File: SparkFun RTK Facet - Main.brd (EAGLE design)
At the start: 60 x 40 mm, 119 parts, among them J17 3-PIN SMD, J18 QWIIC_RIGHT_ANGLE, J2 U.FL, J3 Qwiic, J4 Qwiic Right Angle, Q1 600mA/40V, Q2 MBT3904DW1T1, U1 74HC4052D, U10 MCP73833, U2 3.3V, U3 U-BLOX_ZED-F9P, U4 3.3V, U5 ESP-WROOM-32NARROW, U6 CH340C, U7 MAX17048

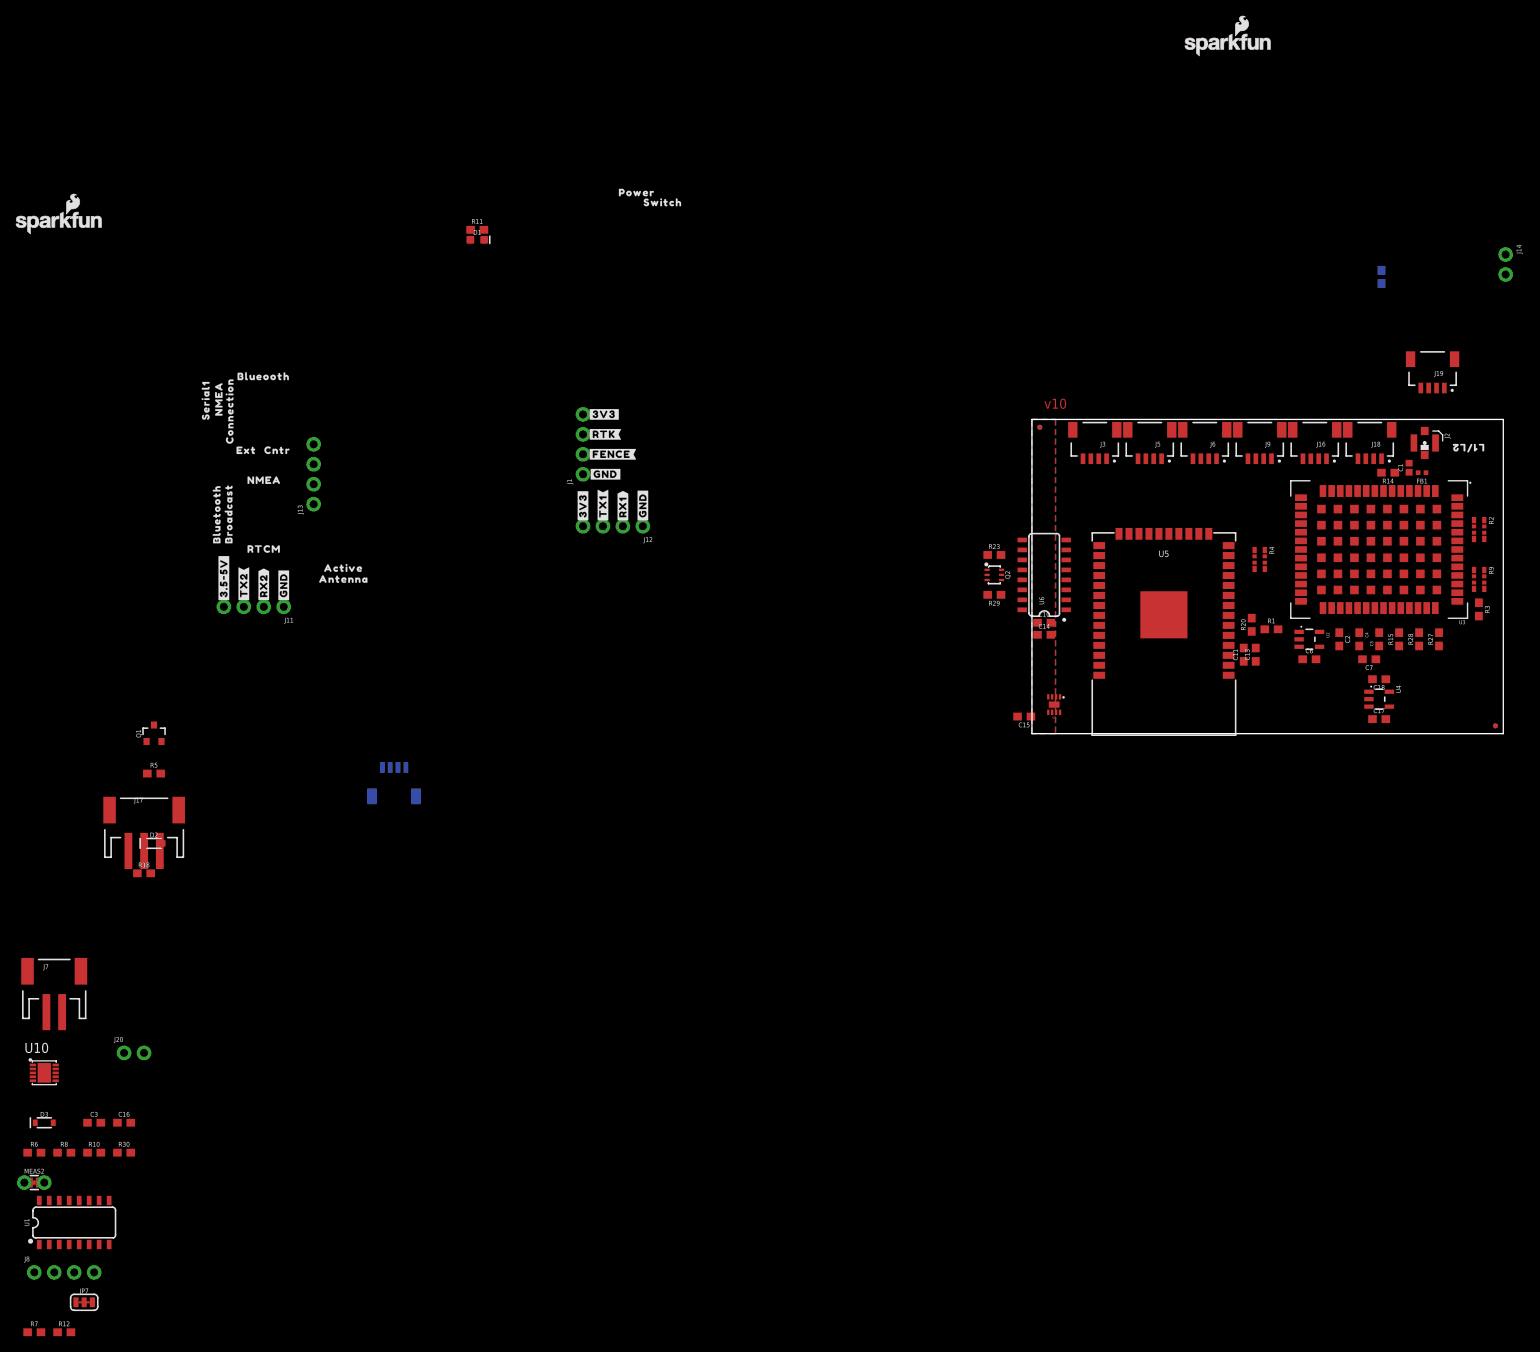
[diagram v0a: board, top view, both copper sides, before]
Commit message: Add 22ohm to USB hub D+/D-.
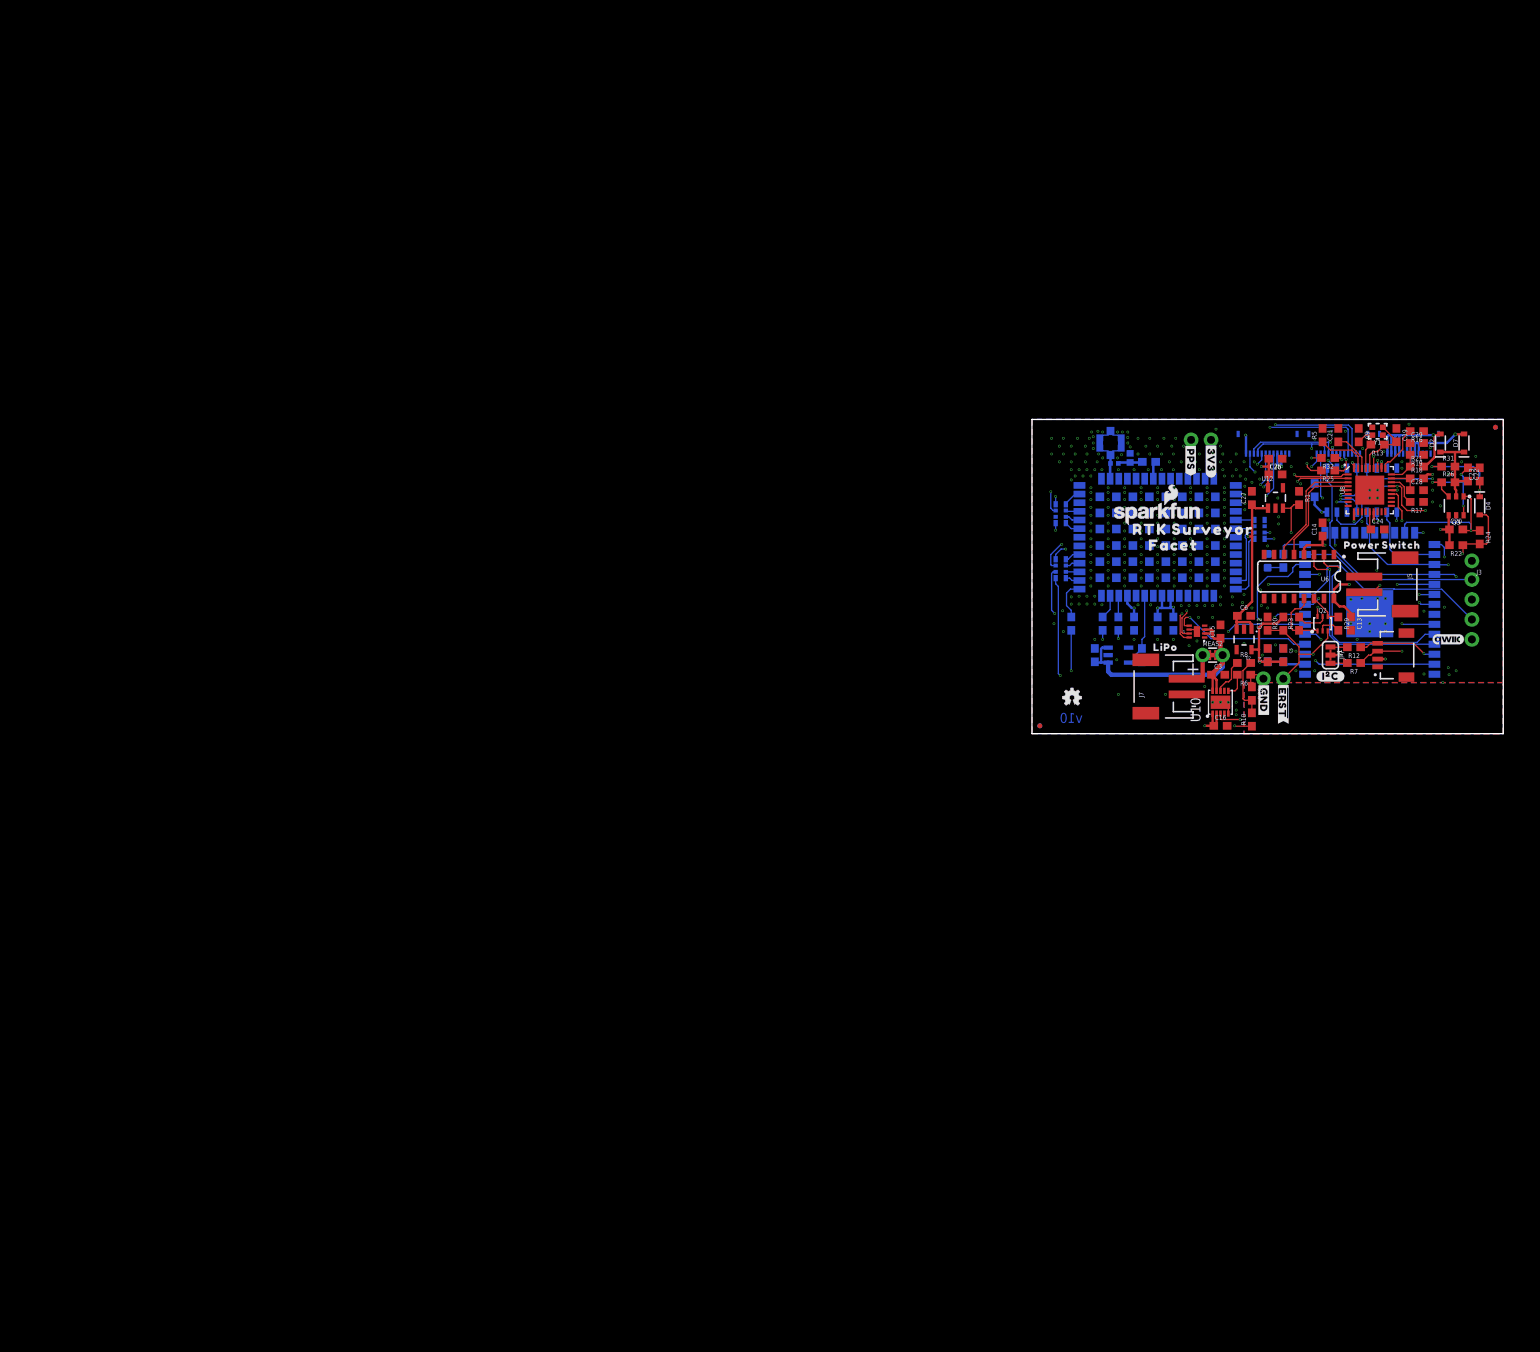
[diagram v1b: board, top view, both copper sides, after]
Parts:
- removed D3: 3A/10V/280mV, SparkFun-DiscreteSemi:SOD-323
- removed J11, J12, J13, J8: (no value), SparkFun-Connectors:1X04_NO_SILK
- removed J16, J19, J9: (no value), SparkFun-Connectors:JST04_1MM_RA
- removed J17: 3-PIN SMD, SparkFun-Connectors:JST-3-SMD
- removed J20: (no value), SparkFun-Connectors:1X02_NO_SILK
- removed Q1: 600mA/40V, SparkFun-DiscreteSemi:SOT23-3
- removed U$27: (no value), output:LIPO0
- removed U$28: (no value), output:##RST##4
- removed U$32: (no value), output:#FENCE#3
- removed U$33: (no value), output:#INT#0
- removed U$37: (no value), output:#3V3#0
- removed U$38, U$82: (no value), output:#GND#0
- removed U$39: (no value), output:#RX2#2
- removed U$40: (no value), output:#TX2#1
- removed U$41: (no value), output:BLUETOOTH2
- removed U$51: (no value), output:BROADCAST3
- removed U$52: (no value), output:NMEA1
- removed U$53: (no value), output:RTCM0
- removed U$56: (no value), output:POWER0
- removed U$57: (no value), output:SWITCH1
- removed U$58: (no value), output:BLUEOOTH3
- removed U$59: (no value), output:CNTR1
- removed U$60: (no value), output:#ESP_RST#0
- removed U$61: (no value), output:EXT0
- removed U$62: (no value), output:NMEA2
- removed U$63: (no value), output:SERIAL10
- removed U$64: (no value), output:CONNECTION1
- removed U$65: (no value), output:#TX1#1
- removed U$68: (no value), output:#RX1#2
- removed U$72: (no value), output:#TX#1
- removed U$73: (no value), output:#DUAL#0
- added C19, C9: 18pF, SparkFun-Capacitors:0603
- added C20: 22uF, SparkFun-Capacitors:0603
- added C21, C22, C23, C24, C26, C28, C29, C8: 0.1uF, SparkFun-Capacitors:0603
- added C25, C27: 1.0uF, SparkFun-Capacitors:0603
- added D4: 250mA/100V, SparkFun-DiscreteSemi:SOD-323
- added D7: 3A/10V/280mV, SparkFun-DiscreteSemi:SOD-323
- added FRAME1: FRAME-LEDGER, SparkFun-Aesthetics:CREATIVE_COMMONS
- added J10, J15: FPC_12_0.5MM2, RTK Facet:FPC_12_FLIP_DOUBLESIDED_2
- added Q3: SIL2308, SparkFun-DiscreteSemi:SOT26
- added R13: 1M, SparkFun-Resistors:0603
- added R16, R17, R19, R21, R26: 100k, SparkFun-Resistors:0603
- added R22, R31: 10k, SparkFun-Resistors:0603
- added R24: 300k, SparkFun-Resistors:0603
- added R25, R32: 22, SparkFun-Resistors:0603
- added U$12: (no value), output:SWITCH1
- added U$13: (no value), output:SW0
- added U$15: (no value), output:RTK0
- added U$20: (no value), output:140
- added U$21: (no value), output:321
- added U$22: (no value), output:332
- added U$24: (no value), output:STAT0
- added U$25: (no value), output:#I�C#0
- added U$26: (no value), output:##ERST##0
- added U$3: (no value), output:EC21
- added U$4: (no value), output:SD#DIS0
- added U$7: (no value), output:ANTENNA2
- added U$8: (no value), output:EC10
- added U$9: (no value), output:L1#L20
- added U12: AP2112K-3.3, SparkFun-IC-Power:SOT23-5
- added U8: USB251XB, USB251xB:QFN-36
- added Y1: 24MHz, SparkFun-Clocks:CRYSTAL-SMD-2.0X1.6MM
- J1: value (none) -> QWIIC_RIGHT_ANGLE; device SparkFun-Connectors:1X04_NO_SILK -> SparkFun-Connectors:JST04_1MM_RA
- J18: value QWIIC_RIGHT_ANGLE -> FPC_12_0.5MM2; device SparkFun-Connectors:JST04_1MM_RA -> RTK Facet:FPC_12_FLIP_DOUBLESIDED_2
- J3: value Qwiic -> (none); device SparkFun-Connectors:JST04_1MM_RA -> SparkFun-Connectors:1X01_NO_SILK
- J4: value Qwiic Right Angle -> (none); device SparkFun-Connectors:JST04_1MM_RA -> SparkFun-Connectors:1X02_NO_SILK
- J5: device SparkFun-Connectors:JST04_1MM_RA -> SparkFun-Connectors:JST-2-SMD
- J6: device SparkFun-Connectors:JST04_1MM_RA -> SparkFun-Connectors:1X04_NO_SILK
- R1, R18: value 1k -> 100k
- R11: value 330 -> 1k
- R5: value 10k -> 12k
- U$1: device output:#GND#0 -> output:LIPO0
- U$10: device output:#RTK#1 -> output:#PPS#1
- U$11: device output:#PPS#0 -> output:POWER0
- U$14: device output:#RX#2 -> output:FACET2
- U$16: device output:ZED0 -> output:SURVEYOR1
- U$17: device output:##SAFE##5 -> output:FACET2
- U$18: device output:ACTIVE0 -> output:SURVEYOR1
- U$19: device output:L1#L21 -> output:RTK0
- U$23: device output:#3#5#5V#0 -> output:I353
- U$5: device output:#3V3#0 -> output:ACTIVE1
- U$6: device output:ANTENNA0 -> output:#3V3#0
- U4: value 3.3V -> ADP160
- moved U1 188.6 mm to (42.0, 31.0), flipped to the bottom, turned to 180 degrees
- moved R7 188.4 mm to (41.0, 9.00), turned to 180 degrees
- moved R12 185.9 mm to (41.0, 11.0), turned to 180 degrees
- moved JP7 178.8 mm to (38.0, 10.0), turned to 270 degrees
- moved D2 171.5 mm to (52.0, 37.0), turned to 90 degrees
- moved R18 169.7 mm to (49.0, 32.5)
- moved R6 165.6 mm to (27.0, 7.50), turned to 180 degrees
- moved MEAS2 164.3 mm to (23.0, 10.0)
- moved R8 162.6 mm to (27.0, 9.00)
- moved R10 157.4 mm to (28.0, 1.80), turned to 90 degrees
- moved U10 157.0 mm to (24.0, 4.00), turned to 90 degrees
- moved U$23 156.6 mm to (53.7, 12.0), flipped to the bottom, turned to 0 degrees
- moved R30 155.0 mm to (28.0, 5.10), turned to 270 degrees
- moved R5 154.9 mm to (37.0, 38.0), turned to 90 degrees
- moved C3 154.0 mm to (23.7, 7.50)
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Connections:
- net ESP_16/ZED-TX01 renamed ESP_16/ZED-TXO1
- removed net 5V: C6.1, D2.C, J11.4, J17.1, U2.1, U2.3
- removed net ESP_12: J8.3, U5.14
- removed net ESP_13: J8.2, U5.16
- removed net ESP_15: U5.23
- removed net ESP_2/MUX_A: U1.10, U5.24
- removed net ESP_32/PWR_LVL_RED: U5.8
- removed net ESP_33/PWR_LVL_GRN: U5.9
- removed net ESP_4/MUX_B: U1.9, U5.26
- removed net ESP_5: J8.4, U5.29
- removed net ESP_D_N: J16.3, U6.6
- removed net ESP_D_P: J16.2, U6.5
- removed net ESP_I35/SWITCH_BASE_SELECT: Q1.3, U5.7
- removed net UBX_D_N: J9.3, R28.1
- removed net UBX_D_P: J9.2, R27.1
- removed net VIN: C16.1, D3.C, J16.1, J17.2, J9.1, U10.1, U10.2
- new net ESP_12/STAT_LED: R11.2, U5.14
- new net ESP_13/POWER_CTRL: D4.A, R22.1, R24.2, U5.16
- new net ESP_15/FAST_OFF: C20.2, Q3.G1, R24.1, U5.23
- new net ESP_2/PERIPHERAL_POWER: R1.2, U12.3, U5.24
- new net ESP_32: J6.3, U5.8
- new net ESP_33: J6.2, U5.9
- new net ESP_3V3: C10.1, C11.1, C4.1, C5.2, R20.2, U2.5, U5.2
- new net ESP_4/MUX_A: U1.10, U5.26
- new net ESP_5/MUX_B: U1.9, U5.29
- new net ESP_DM: U6.6, U8.3
- new net ESP_DP: U6.5, U8.4
- new net ESP_I35: J6.1, U5.7
- new net N$10: R16.2, U8.28
- new net N$14: R17.2, U8.25
- new net N$19: R25.2, U8.30
- new net N$20: R32.2, U8.31
- new net N$5: R2.P2, U3.51
- new net N$6: C22.1, C23.2, Q3.D1, Q3.G2, R26.1
- new net N$7: C9.2, R13.2, U8.33, Y1.3
- new net N$9: R5.1, U8.35
- new net POWER_BTN: C23.1, D4.C, J3.1, J5.2, R31.1
- new net USB_!RESET: C28.1, R18.1, U8.26
- new net USB_DM: J18.8, R25.1
- new net USB_DP: J18.7, R32.1
- new net VBUS_DET: C29.1, R19.2, R21.1, U8.27
- new net VOUT: C20.1, C27.1, C6.1, Q3.D2, R22.2, U12.1, U2.1, U2.3
- new net V_RAW: C16.1, C22.2, D2.C, D7.C, Q3.S2, R26.2, R31.2, U10.1, U10.2
- new net V_USB: D2.A, J10.1, J15.1, J15.2, J15.3, J15.4, R21.2
- new net ZED_DM: R28.1, U8.1
- new net ZED_DP: R27.1, U8.2
- new net ZED_EXTINT: R2.P7, U1.5
- net 3.3V: now also C25.1, C26.2, C8.1, J1.2, J10.10, J10.9, J18.5, J18.6, J4.1, R18.2, U12.5, U8.10, U8.15, U8.23, U8.29, U8.36, U8.5; no longer C10.1, C11.1, C4.1, C5.2, J1.4, J12.4, J18.2, J3.2, J4.2, R20.2, U2.5, U5.2
- net CHG_LED: now also J10.2; no longer R1.2
- net ESP_14: now also J6.4; no longer J8.1
- net ESP_18/SD_SCK: now also J10.6; no longer J19.3
- net ESP_19/SD_CIPO: now also J10.5; no longer J19.4
- net ESP_21/SDA: now also J1.3, J10.3, J18.4, U8.22; no longer J18.3, J3.3, J4.3
- net ESP_22/SCL: now also J1.4, J10.4, J18.3, U8.24; no longer J18.4, J3.4, J4.4
- net ESP_23/SD_COPI: now also J10.7; no longer J19.2
- net ESP_25/SD_!CS!: now also J10.8; no longer J19.1
- net ESP_27/ZED_!RESET!: no longer J13.3, U1.5
- net ESP_I34/ZED_TX_READY: no longer J13.4
- net EXTERNAL_SERIAL1_RXI: now also J18.1; no longer J12.2, J5.1
- net EXTERNAL_SERIAL1_TXO: now also J18.2; no longer J12.3, J5.2
- net GND: now also C19.1, C21.2, C24.2, C25.2, C26.1, C27.2, C28.2, C29.2, C8.2, C9.1, J10.11, J10.12, J15.10, J15.11, J15.12, J18.11, J18.12, J5.1, Q3.S1, R1.1, R16.1, R17.1, R19.1, R5.2, U12.2, U8.11, U8.EP; no longer J11.1, J12.1, J16.4, J18.1, J20.2, J3.1, J4.1, J6.1, J6.2, J9.4, Q1.2, R5.1
- net N$15: now also C21.1, U8.34; no longer D2.A, J17.3, R18.1
- net N$17: now also C24.1, U8.14; no longer R1.1
- net N$8: now also C19.2, R13.1, U8.32, Y1.1; no longer Q1.1, R18.2, R5.2
- net V_BATT: now also D7.A, J15.6, J15.7, J15.8, J15.9; no longer D3.A, J20.1, J6.3, J6.4
- net ZED-RXI2: now also J18.9; no longer J11.2, J5.3
- net ZED-TXO2: now also J18.10; no longer J11.3, J5.4
- net ZED_!SAFE!: no longer J13.2
- net ZED_FENCE_STAT: no longer J1.2
- net ZED_PPS_STAT: now also J4.2; no longer J13.1, R11.2
- net ZED_RTK_STAT: no longer J1.3
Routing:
- net ESP_22/SCL: track 0.00 -> 136.5 mm, vias 0 -> 9
- net ESP_21/SDA: track 0.00 -> 121.1 mm, vias 0 -> 9
- net V_BATT: track 0.00 -> 107.6 mm, vias 0 -> 2
- net ESP_17/ZED-RXI1: track 0.00 -> 103.9 mm, vias 0 -> 3
- net ESP_16/ZED-TXO1: track 0.00 -> 82.4 mm, vias 0 -> 3
- net V_RAW: track 0.00 -> 78.3 mm, vias 0 -> 3
- net ZED_EXTINT: track 0.00 -> 75.7 mm, vias 0 -> 3
- net ZED_PPS_STAT: track 0.00 -> 58.1 mm, vias 0 -> 4
- net ZED_DP: track 0.00 -> 56.7 mm, vias 0 -> 3
- net ZED_DM: track 0.00 -> 56.3 mm, vias 0 -> 3
- net VOUT: track 0.00 -> 52.2 mm, vias 0 -> 2
- net ESP_27/ZED_!RESET!: track 0.00 -> 51.4 mm, vias 0 -> 3
- net ESP_23/SD_COPI: track 0.00 -> 48.5 mm, vias 0 -> 3
- net V_USB: track 0.00 -> 47.3 mm, vias 0 -> 2
- net 3.3V: track 0.00 -> 46.2 mm, vias 0 -> 19
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- added copper zone on layer 15, net 3.3V

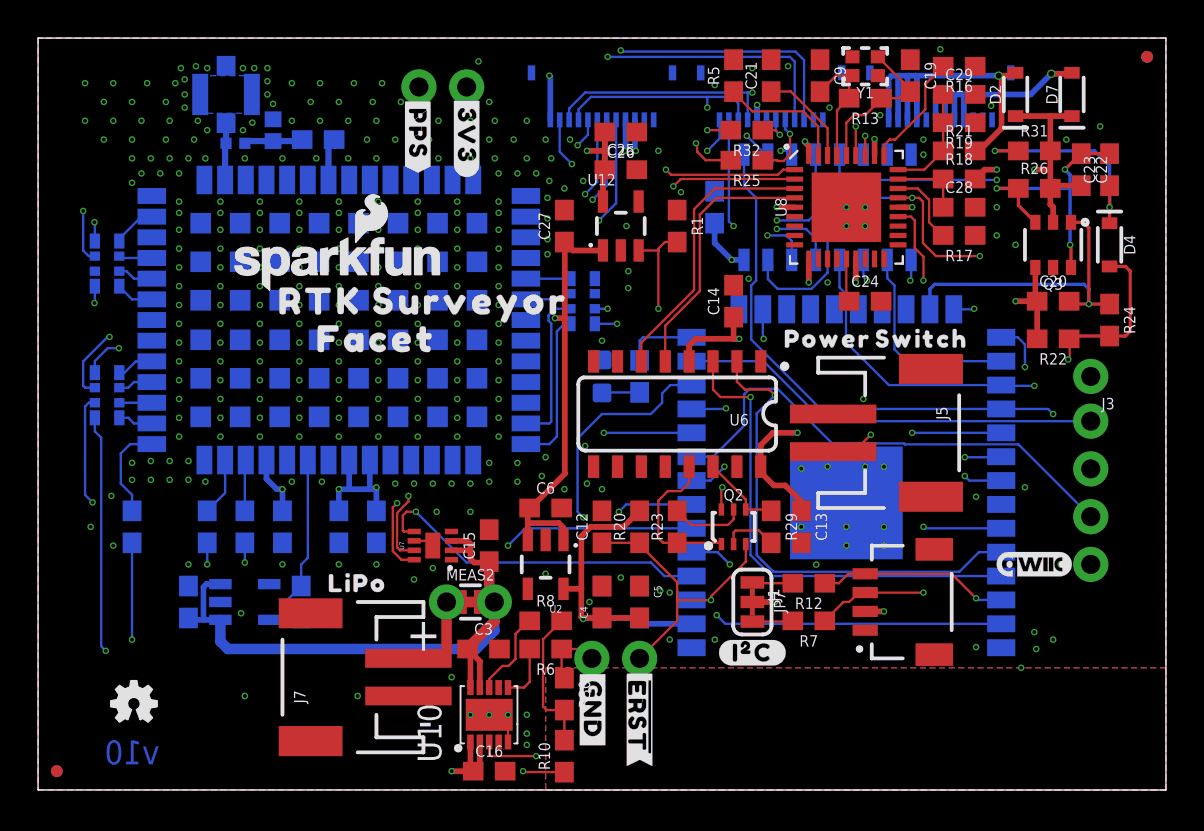
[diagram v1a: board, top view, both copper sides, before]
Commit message: Fix errors on all 3 boards after enclosure review.
* Flip connector board completely. Mirror connectors.
* Mirror connector on SD board
* Move LED above SIM socket
* Add membrane connector to SD board
* Remove switch connector from main board
* Increase width of connector board, 2mm on each side - 54mm wide
* Move LiPo Connector north as much as possible
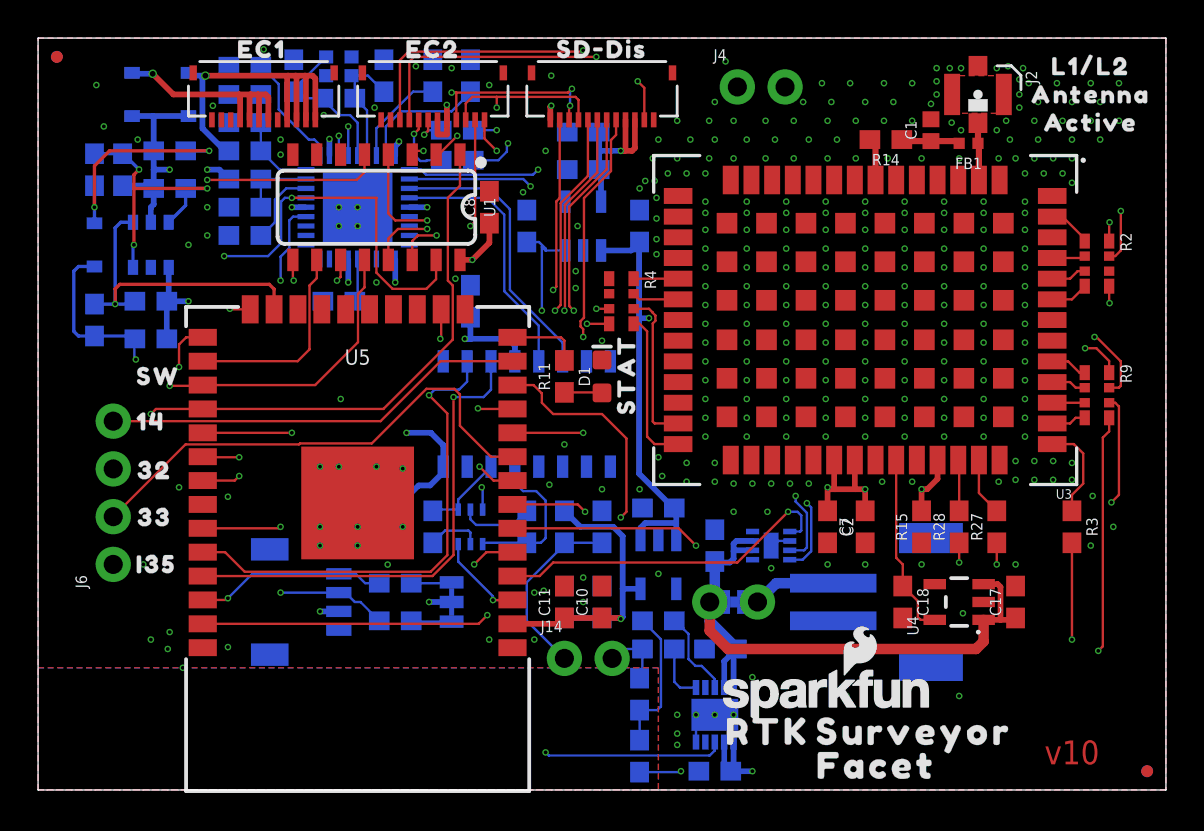
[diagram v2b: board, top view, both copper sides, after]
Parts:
- removed J3: (no value), SparkFun-Connectors:1X01_NO_SILK
- removed J5: (no value), SparkFun-Connectors:JST-2-SMD
- removed U$11: (no value), output:POWER0
- removed U$12: (no value), output:SWITCH1
- moved FRAME1 104.1 mm to (82.0, 6.00), flipped to the top
- moved FRAME2 104.1 mm to (82.0, 6.00), flipped to the top
- moved U$2 65.1 mm to (62.5, 81.3), flipped to the top
- moved JP21 58.0 mm to (59.0, 1.00), flipped to the top
- moved JP61 58.0 mm to (1.00, 39.0), flipped to the top
- moved JP71 58.0 mm to (59.0, 1.00), flipped to the bottom
- moved JP81 58.0 mm to (1.00, 39.0), flipped to the bottom
- moved C23 54.0 mm to (3.00, 33.0), flipped to the bottom
- moved D4 54.0 mm to (3.00, 29.0), flipped to the bottom
- moved R24 54.0 mm to (3.00, 25.0), flipped to the bottom
- moved R2 52.6 mm to (56.3, 28.0), flipped to the top
- moved R9 52.6 mm to (56.3, 21.0), flipped to the top
- moved J6 52.0 mm to (4.00, 12.0), flipped to the top
- moved U$5 52.0 mm to (56.0, 35.5), flipped to the top
- moved U$7 52.0 mm to (56.0, 37.0), flipped to the top
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- renumbered J10 to J8
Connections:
- net 3.3V: now also J8.3, J8.4; no longer J8.10, J8.9
- net CHG_LED: now also J8.11; no longer J8.2
- net ESP_18/SD_SCK: now also J8.7; no longer J8.6
- net ESP_19/SD_CIPO: now also J8.8; no longer J8.5
- net ESP_21/SDA: now also J8.10; no longer J8.3
- net ESP_22/SCL: now also J8.9; no longer J8.4
- net ESP_23/SD_COPI: now also J8.6; no longer J8.7
- net ESP_25/SD_!CS!: now also J8.5; no longer J8.8
- net GND: now also J8.1; no longer J5.1, J8.11, J8.12
- net POWER_BTN: now also J8.2; no longer J3.1, J5.2
- net V_USB: now also J8.12; no longer J8.1
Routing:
- net POWER_BTN: track 38.0 -> 49.8 mm, vias 3 -> 4
- net CHG_LED: track 38.1 -> 43.9 mm
- net V_USB: track 47.3 -> 41.8 mm, vias 2 -> 3
- net ESP_19/SD_CIPO: track 42.2 -> 39.0 mm
- net ESP_21/SDA: track 121.1 -> 118.6 mm, vias 9 -> 11
- net ESP_18/SD_SCK: track 40.0 -> 37.5 mm
- net ESP_22/SCL: track 136.5 -> 134.3 mm
- net 3.3V: track 46.2 -> 47.0 mm, vias 19 -> 17
- net ESP_23/SD_COPI: track 48.5 -> 47.6 mm
- net ESP_25/SD_!CS!: track 22.0 -> 21.3 mm
- net GND: vias 292 -> 290
